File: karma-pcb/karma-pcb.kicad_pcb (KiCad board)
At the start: 2 copper layers, 126.6 x 103.9 mm, 82 parts, among them J1 BAT, J2 BAT, U1 xiao-ble, U2 xiao-ble

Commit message: Add left side pcb design rev 0.1
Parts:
- added REF**: MountingHole_3.2mm_M3_DIN965_Pad, MountingHole:MountingHole_3.2mm_M3_DIN965_Pad, F.Cu at (279.2, 109.3)
- added REF**: MountingHole_3.2mm_M3_DIN965_Pad, MountingHole:MountingHole_3.2mm_M3_DIN965_Pad, F.Cu at (181.0, 34.1)
- added REF**: MountingHole_3.2mm_M3_DIN965_Pad, MountingHole:MountingHole_3.2mm_M3_DIN965_Pad, F.Cu at (255.0, 33.5)
- added REF**: MountingHole_3.2mm_M3_DIN965_Pad, MountingHole:MountingHole_3.2mm_M3_DIN965_Pad, F.Cu at (181.0, 100.6)
- DR1, DR10, DR11, DR12, DR13, DR14, DR15, DR16, DR17, DR18, DR2, DR3, DR4, DR5, DR6, DR7, DR8, DR9: moved to B.Cu
- moved RSW2 120.7 mm to (245.7, 33.2)
- moved DR5 111.7 mm to (275.2, 64.8), turned to 90 degrees
- moved DR4 110.9 mm to (256.7, 50.9), turned to 90 degrees
- moved DR3 107.6 mm to (238.2, 43.9), turned to 90 degrees
- moved DR9 105.8 mm to (256.7, 69.4), turned to 90 degrees
- moved DR8 102.2 mm to (238.2, 62.4), turned to 90 degrees
- moved DR2 94.0 mm to (219.7, 50.9), turned to 90 degrees
- moved SWR16 91.8 mm to (171.5, 120.0), turned to 30 degrees
- moved DR7 88.3 mm to (219.7, 69.4), turned to 90 degrees
- moved DR10 86.6 mm to (275.2, 83.2), turned to 90 degrees
- moved DR1 85.6 mm to (201.2, 55.5), turned to 90 degrees
- moved U2 84.9 mm to (272.8, 40.5), turned to -90 degrees
- moved DR15 82.9 mm to (275.2, 101.8), turned to 90 degrees
- moved DR6 79.9 mm to (201.2, 74.0), turned to 90 degrees
- moved DR14 78.3 mm to (256.7, 87.9), turned to 90 degrees
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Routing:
- net COL4_R: track 0.00 -> 223.8 mm
- net COL3_R: track 0.00 -> 205.6 mm, vias 0 -> 5
- net ROW3_R: track 0.00 -> 178.9 mm
- net COL2_R: track 0.00 -> 176.3 mm, vias 0 -> 5
- net ROW2_R: track 0.00 -> 169.9 mm, vias 0 -> 2
- net ROW1_R: track 0.00 -> 151.8 mm, vias 0 -> 2
- net ROW0_R: track 0.00 -> 133.8 mm, vias 0 -> 2
- net COL1_R: track 0.00 -> 107.0 mm, vias 0 -> 4
- net COL0_R: track 0.00 -> 97.0 mm, vias 0 -> 4
- net VBAT_R: track 0.00 -> 85.1 mm
- net RESET_R: track 0.00 -> 47.1 mm
- net COL3_L: track 162.8 -> 185.7 mm, vias 7 -> 3
- net COL4_L: track 184.2 -> 206.7 mm, vias 7 -> 3
- net COL2_L: track 143.6 -> 164.9 mm, vias 7 -> 3
- net Net-(DR16-A): track 0.00 -> 20.3 mm
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- added copper zone on F.Cu, net GND_R
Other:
- board size 126.6 x 103.9 mm -> 255.5 x 103.3 mm

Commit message: Fix board edge DRC failures on the left side
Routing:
- net COL1_R: track 107.0 -> 110.1 mm
- net RESET_R: track 47.1 -> 46.0 mm
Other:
- outline, holes or cut-outs redrawn

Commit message: Fix board edge DRC failures on the right side
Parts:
- moved REF** 0.58 mm to (255.0, 34.1)
- moved REF** 0.58 mm to (56.1, 34.1)
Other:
- outline, holes or cut-outs redrawn

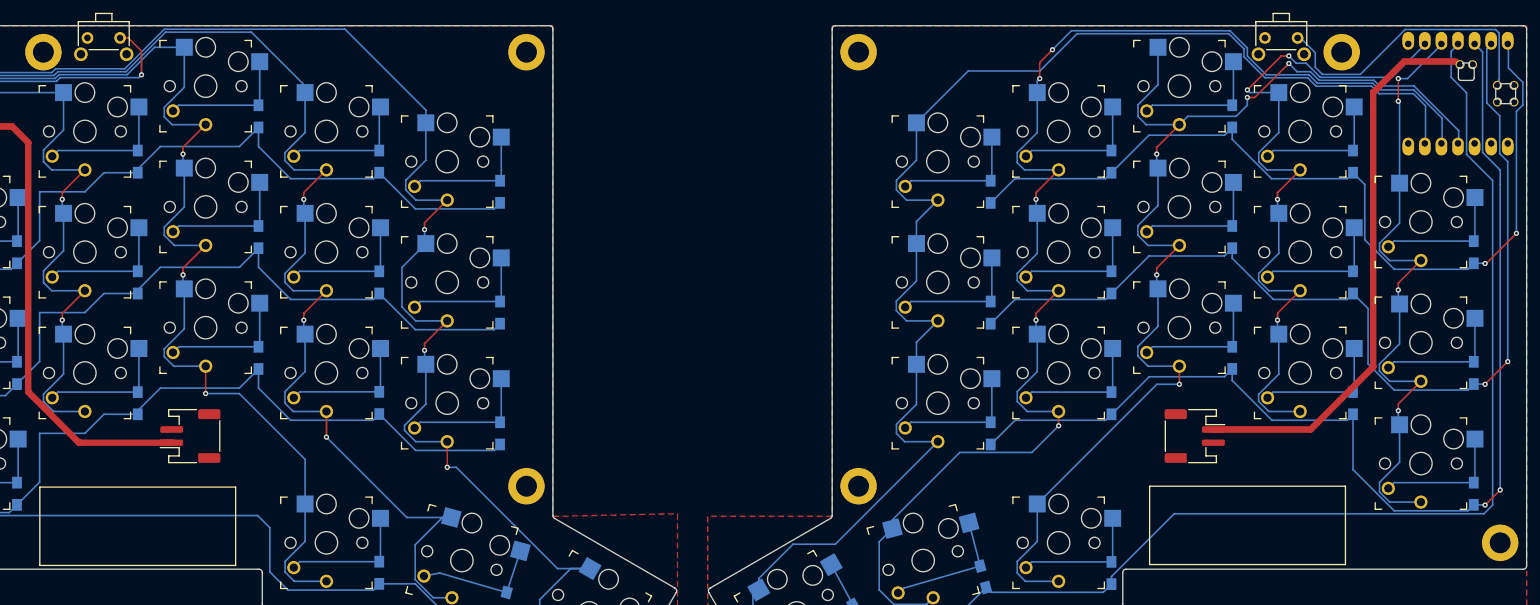
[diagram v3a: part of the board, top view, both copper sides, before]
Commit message: Fix positioning of the controller on the right pcb
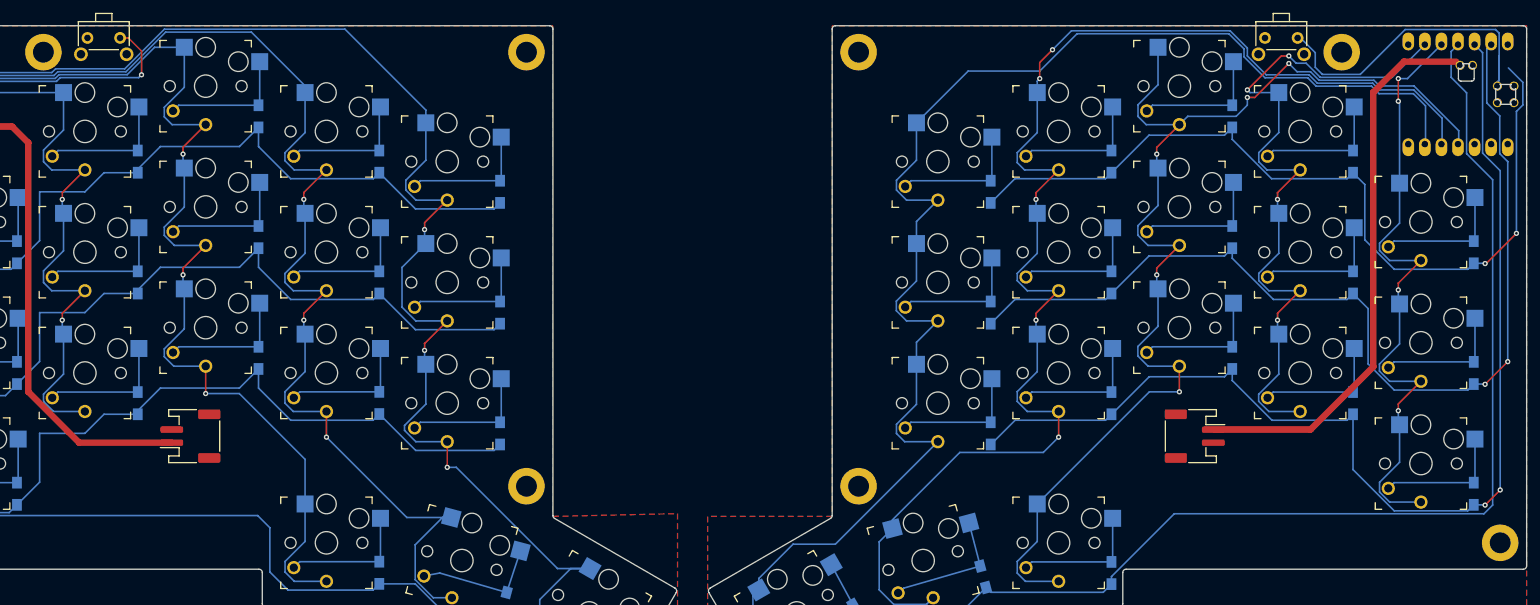
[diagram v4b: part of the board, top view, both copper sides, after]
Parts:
- moved U2 0.10 mm to (272.8, 40.6)
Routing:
- net RESET_R: track 46.0 -> 50.3 mm
- net ROW0_R: track 133.8 -> 130.1 mm
- net COL3_R: track 205.6 -> 206.7 mm
- net COL2_R: track 176.6 -> 177.5 mm

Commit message: Improve trace routing
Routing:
- net COL2_L: track 164.8 -> 173.8 mm
- net COL2_R: track 177.5 -> 183.9 mm
- net COL4_R: track 223.9 -> 228.8 mm
- net COL3_R: track 206.7 -> 211.6 mm
- net COL0_L: track 78.5 -> 83.1 mm
- net COL3_L: track 186.2 -> 190.8 mm
- net COL1_R: track 110.0 -> 114.5 mm
- net COL4_L: track 207.1 -> 211.5 mm
- net ROW0_R: track 130.1 -> 133.7 mm
- net COL0_R: track 96.9 -> 100.5 mm
- net VBAT_L: track 79.7 -> 76.7 mm
- net COL1_L: track 93.9 -> 96.2 mm
- net ROW2_L: track 181.7 -> 182.4 mm
- net ROW1_L: track 160.7 -> 161.4 mm
- net ROW0_L: track 134.9 -> 135.6 mm
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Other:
- board text added: "BATTERY"
